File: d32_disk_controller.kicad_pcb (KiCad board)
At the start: 2 copper layers, 136.4 x 80.3 mm, 25 parts, among them J1 Clock_Test, J2 IDC_Floppy, J3 EDGE, U1 27C64, U2 WD2797, U3 74LS174, U4 74LS139, U5 74LS00, U6 7416, U7 7417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

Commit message: redraft traces
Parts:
- moved U7 39.7 mm to (122.9, 62.5)
- moved U6 31.8 mm to (131.6, 75.2)
- moved RN1 31.2 mm to (140.5, 71.4)
- moved J2 29.0 mm to (145.8, 62.0)
- moved U2 28.5 mm to (102.9, 70.6)
- moved U8 24.8 mm to (122.9, 51.3)
- moved R9 18.3 mm to (125.5, 89.9)
- moved C7 17.8 mm to (130.0, 110.7)
- moved U1 15.5 mm to (72.9, 85.3)
- moved C2 10.2 mm to (129.5, 105.2), turned to 0 degrees
- moved J1 8.84 mm to (136.9, 93.5)
- moved R8 8.78 mm to (131.6, 92.5), turned to 0 degrees
- moved R10 8.35 mm to (125.5, 99.8)
- moved D1 5.89 mm to (131.6, 100.6)
- moved R3 4.86 mm to (131.6, 97.2)
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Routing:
- net GND: track 593.4 -> 102.1 mm, vias 2 -> 5
- net +5V: track 353.3 -> 0.00 mm, vias 11 -> 0
- net ~{NMI}: track 162.0 -> 0.00 mm, vias 1 -> 0
- net P2: track 141.8 -> 0.00 mm, vias 1 -> 0
- net D0: track 138.4 -> 0.00 mm, vias 2 -> 0
- net D3: track 135.5 -> 0.00 mm, vias 2 -> 0
- net D4: track 132.8 -> 0.00 mm, vias 1 -> 0
- net MOTOR: track 131.6 -> 0.00 mm, vias 1 -> 0
- net D5: track 130.3 -> 0.00 mm, vias 2 -> 0
- net D2: track 127.1 -> 0.00 mm, vias 2 -> 0
- net D1: track 120.5 -> 0.00 mm, vias 3 -> 0
- net D6: track 112.1 -> 0.00 mm, vias 1 -> 0
- net D7: track 106.0 -> 0.00 mm, vias 2 -> 0
- net Net-(U3-Q2): track 105.3 -> 0.00 mm, vias 2 -> 0
- net Net-(U5-Pad3): track 99.8 -> 0.00 mm, vias 4 -> 0
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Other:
- board size 136.4 x 80.3 mm -> 107.5 x 80.3 mm

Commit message: rework traces
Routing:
- net +5V: track 0.00 -> 412.3 mm, vias 0 -> 19
- net GND: track 102.1 -> 353.6 mm, vias 5 -> 17
- net ~{RESET}: track 0.00 -> 105.3 mm, vias 0 -> 5
- net MOTOR: track 0.00 -> 88.7 mm, vias 0 -> 6
- net Net-(U3-Q2): track 0.00 -> 82.6 mm, vias 0 -> 6
- net STEP: track 0.00 -> 74.4 mm, vias 0 -> 3
- net ~{WPRT}: track 0.00 -> 74.0 mm, vias 0 -> 4
- net CLK: track 0.00 -> 65.7 mm, vias 0 -> 2
- net DIRC: track 0.00 -> 59.9 mm, vias 0 -> 1
- net D1: track 0.00 -> 56.8 mm, vias 0 -> 2
- net D0: track 0.00 -> 56.7 mm, vias 0 -> 2
- net D2: track 0.00 -> 56.6 mm, vias 0 -> 2
- net ~{IP}: track 0.00 -> 55.4 mm, vias 0 -> 4
- net Net-(U4A-O3): track 0.00 -> 54.6 mm, vias 0 -> 4
- net /raw_clock: track 0.00 -> 52.4 mm, vias 0 -> 4
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
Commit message: revise tracing
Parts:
- moved C1 8.65 mm to (86.1, 68.1)
- moved Y1 1.02 mm to (91.2, 68.0)
- moved R1 0.93 mm to (96.7, 70.1)
- moved R2 0.73 mm to (96.8, 62.5)
- moved C8 0.20 mm to (96.7, 66.3)
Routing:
- net GND: track 353.6 -> 511.2 mm, vias 17 -> 27
- net P2: track 0.00 -> 115.7 mm, vias 0 -> 3
- net R/~{W}: track 0.00 -> 85.5 mm, vias 0 -> 3
- net A3: track 31.2 -> 108.1 mm, vias 3 -> 6
- net CART: track 0.00 -> 73.3 mm, vias 0 -> 3
- net INTR0: track 0.00 -> 72.8 mm, vias 0 -> 4
- net D5: track 28.8 -> 99.2 mm, vias 2 -> 5
- net D4: track 33.7 -> 101.7 mm, vias 2 -> 6
- net D0: track 56.7 -> 122.4 mm, vias 2 -> 6
- net D3: track 39.2 -> 103.7 mm, vias 2 -> 5
- net D1: track 56.8 -> 121.0 mm, vias 2 -> 5
- net D2: track 56.6 -> 119.8 mm, vias 2 -> 6
- net ~{NMI}: track 0.00 -> 62.9 mm, vias 0 -> 1
- net +5V: track 412.3 -> 472.4 mm, vias 19 -> 26
- net D6: track 24.3 -> 81.3 mm, vias 2 -> 4
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
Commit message: verify component availability
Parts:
- U3: value 74LS174 -> 74HCT174; footprint Package_SO:SOIC-16W_7.5x10.3mm_P1.27mm -> Package_SO:SOIC-16W_5.3x10.2mm_P1.27mm
- U4: value 74LS139 -> 74HCT139; footprint Package_SO:SOIC-16W_7.5x10.3mm_P1.27mm -> Package_SO:SOIC-16W_5.3x10.2mm_P1.27mm
- U5: value 74LS00 -> 74HCT00; footprint Package_SO:SOIC-14W_7.5x9mm_P1.27mm -> Package_SO:SOIC-14_3.9x8.7mm_P1.27mm
- U6: value 7416 -> 74HCT04; footprint Package_SO:SOIC-14W_7.5x9mm_P1.27mm -> Package_SO:SOIC-14_3.9x8.7mm_P1.27mm
- U7: value 7417 -> 74LS07; footprint Package_SO:SOIC-14W_7.5x9mm_P1.27mm -> Package_SO:SOIC-14_3.9x8.7mm_P1.27mm
- U8: value 74LS74 -> 74HCT74; footprint Package_SO:SOIC-14W_7.5x9mm_P1.27mm -> Package_SO:SOIC-14_3.9x8.7mm_P1.27mm
- U9: value 74LS04 -> 74HCT04; footprint Package_SO:SOIC-14W_7.5x9mm_P1.27mm -> Package_SO:SOIC-14_3.9x8.7mm_P1.27mm
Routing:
- net GND: track 511.2 -> 525.5 mm
- net Net-(U8A-C): track 16.1 -> 10.0 mm
- net Net-(U5-Pad12): track 7.61 -> 12.0 mm
- net CLK: track 65.7 -> 70.1 mm
- net Net-(U5-Pad9): track 12.2 -> 16.5 mm
- net Net-(U3-Q1): track 54.9 -> 59.2 mm, vias 4 -> 2
- net Net-(U4B-O2): track 43.5 -> 39.3 mm
- net INT: track 22.5 -> 18.5 mm
- net Q: track 45.1 -> 42.0 mm, vias 4 -> 2
- net Net-(U4A-O3): track 53.3 -> 50.6 mm
- net INTR0: track 72.8 -> 70.1 mm
- net Net-(U3-Cp): track 26.0 -> 28.7 mm
- net Net-(U4A-O0): track 44.2 -> 41.6 mm
- net Net-(U4A-O2): track 25.1 -> 27.6 mm
- net DS1: track 27.9 -> 30.2 mm
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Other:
- board text added: "Dragon 32/64 Disk Controller"
- board text added: "V0.0.2-draft"

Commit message: update version
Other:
- board text added: "V0.0.3-draft"
- board text removed: "V0.0.2-draft"
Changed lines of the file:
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@@
     (title "Dragon 32/64 Disk Controller")
     (date "2023-07-06")
-    (rev "V0.0.2")
+    (rev "V0.0.3-draft")
   )
   (layers
@@
   (gr_line (start 63.6524 110.4392) (end 64.2112 110.4392)
     (stroke (width 0.1) (type default)) (layer "Edge.Cuts"))
-  (gr_text "V0.0.2-draft" (at 130.048 51.054) (layer "F.SilkS")
+  (gr_text "V0.0.3-draft" (at 130.048 51.054) (layer "F.SilkS")
     (effects (font (size 1 1) (thickness 0.15)) (justify left bottom))
   )

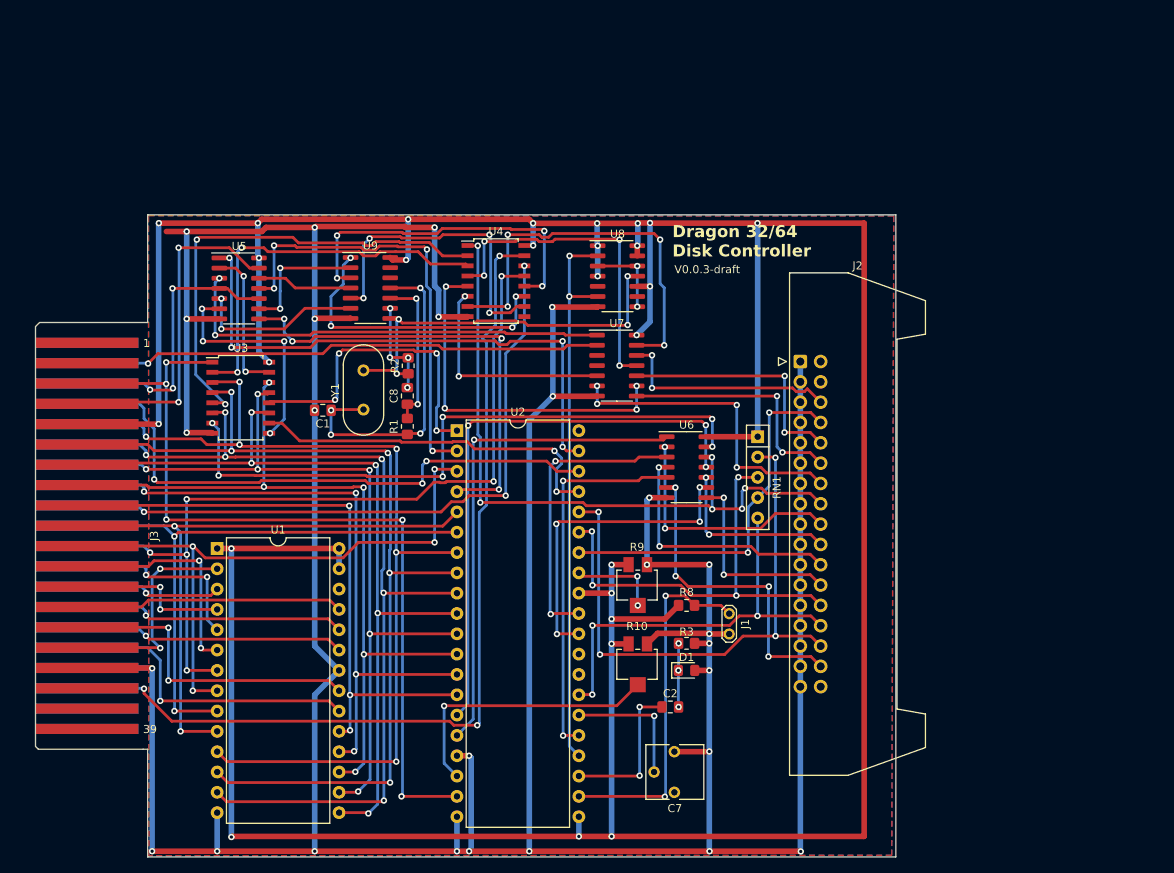
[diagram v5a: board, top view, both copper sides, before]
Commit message: revise board for better component selection
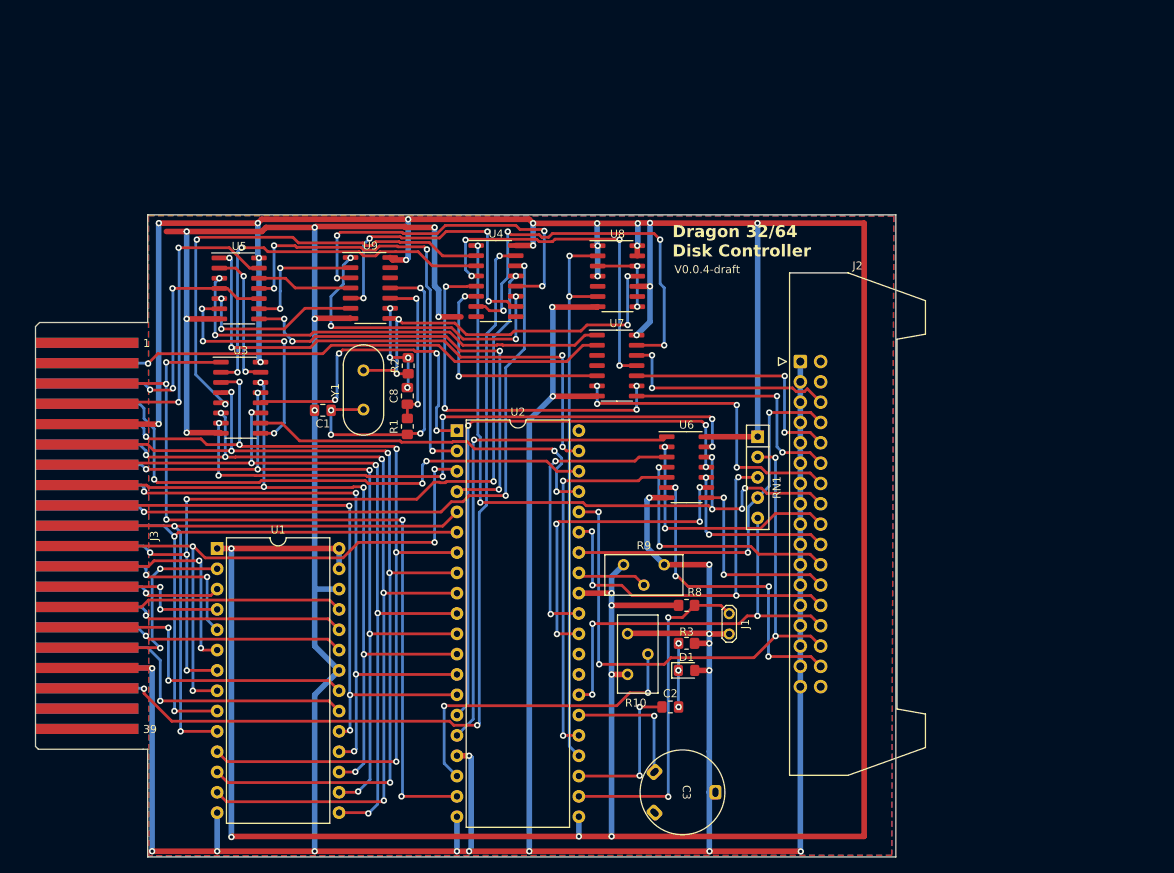
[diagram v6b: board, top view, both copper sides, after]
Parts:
- removed C7: 8-70pF, Potentiometer_THT:Potentiometer_Vishay_T73YP_Vertical
- added C3: 5.5-65pf, d32_cart:Trimmer-10mm, F.Cu at (131.1, 115.8)
- R10, R9: footprint Potentiometer_SMD:Potentiometer_Bourns_3224X_Vertical -> Potentiometer_THT:Potentiometer_Bourns_3296Y_Vertical
- U3, U4: footprint Package_SO:SOIC-16W_5.3x10.2mm_P1.27mm -> Package_SO:SOIC-16_3.9x9.9mm_P1.27mm
- moved R9 4.17 mm to (128.8, 87.4)
- moved R10 4.03 mm to (124.2, 96.0), turned to 90 degrees
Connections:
- U1 pad 26: unconnected-(U1-NC-Pad26) -> GND
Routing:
- net Net-(U2-RPW): track 34.7 -> 40.4 mm, vias 1 -> 2
- net ~{TEST}: track 44.8 -> 42.3 mm
- net Net-(U2-WPW): track 11.2 -> 8.76 mm, vias 2 -> 0
- net Net-(U4B-O2): track 39.3 -> 37.1 mm
- net A3: track 106.4 -> 104.3 mm
- net ~{WPRT}: track 74.0 -> 75.8 mm
- net D2: track 118.7 -> 117.0 mm
- net P2: track 114.4 -> 112.9 mm
- net Net-(U3-Cp): track 28.7 -> 30.2 mm
- net Net-(U4A-O2): track 27.6 -> 29.0 mm
- net ~{NMI}: track 65.1 -> 66.4 mm
- net MOTOR: track 86.8 -> 85.6 mm
- net Net-(U4A-O0): track 41.6 -> 42.8 mm
- net Net-(U4B-O1): track 37.6 -> 38.8 mm
- net ~{RE}: track 57.3 -> 56.0 mm
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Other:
- board text added: "V0.0.4-draft"
- board text removed: "V0.0.3-draft"

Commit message: prepare for cpld
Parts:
- removed C1: 22pF, Capacitor_SMD:C_0805_2012Metric_Pad1.18x1.45mm_HandSolder
- removed C8: 10nF, Capacitor_SMD:C_0805_2012Metric_Pad1.18x1.45mm_HandSolder
- removed R1, R2: 1K, Resistor_SMD:R_0805_2012Metric_Pad1.20x1.40mm_HandSolder
- Y1: footprint Crystal:Crystal_HC18-U_Vertical -> Oscillator:Oscillator_SMD_Abracon_ASV-4Pin_7.0x5.1mm
- moved Y1 53.5 mm to (129.6, 30.6)
- moved C2 25.9 mm to (129.2, 79.2), turned to 180 degrees
- moved C3 25.5 mm to (128.7, 90.4)
- moved J1 24.9 mm to (134.5, 68.7)
- moved R9 24.9 mm to (126.4, 62.6)
- moved U3 24.9 mm to (73.5, 41.7)
- moved J2 24.9 mm to (143.4, 37.2)
- moved J3 24.9 mm to (63.1, 59.0)
- moved U4 24.9 mm to (105.4, 27.1)
- moved U5 24.9 mm to (73.3, 28.0)
- moved U7 24.9 mm to (120.5, 37.7)
- moved U8 24.9 mm to (120.5, 26.5)
- moved U9 24.9 mm to (89.7, 28.0)
- moved R10 24.9 mm to (121.8, 71.2)
- moved U1 24.9 mm to (70.5, 60.5)
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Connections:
- J3 pad 37: unconnected-(J3-Pin_37-Pad37) -> A13
- RN1 pad 2: ~{WPRT} -> ~{IP}
- RN1 pad 3: ~{IP} -> ~{TR00}
- RN1 pad 4: ~{TR00} -> ~{WPRT}
- U1 pad 26: GND -> A13
- U9 pad 10: Net-(C8-Pad1) -> unconnected-(U9-Pad10)
- U9 pad 11: Net-(C1-Pad1) -> unconnected-(U9-Pad11)
- U9 pad 8: /raw_clock -> unconnected-(U9-Pad8)
- U9 pad 9: Net-(C8-Pad2) -> unconnected-(U9-Pad9)
- Y1 pad 1: Net-(C1-Pad1) -> unconnected-(Y1-EN-Pad1)
- Y1 pad 2: /raw_clock -> GND
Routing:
- net GND: track 524.7 -> 32.1 mm, vias 25 -> 11
- net +5V: track 473.7 -> 30.4 mm, vias 25 -> 14
- net A13: track 0.00 -> 52.4 mm, vias 0 -> 2
- net /raw_clock: track 51.1 -> 5.19 mm, vias 4 -> 0
- net Net-(C1-Pad1): track 40.8 -> 0.00 mm, vias 4 -> 0
- net Net-(C8-Pad1): track 19.6 -> 0.00 mm, vias 2 -> 0
- net ENP: track 40.5 -> 26.0 mm, vias 4 -> 0
- net Net-(C8-Pad2): track 12.3 -> 0.00 mm, vias 4 -> 0
- net Net-(U4A-O3): track 50.7 -> 62.7 mm, vias 4 -> 2
- net ~{WPRT}: track 75.8 -> 65.2 mm, vias 4 -> 1
- net Net-(U3-Q2): track 80.2 -> 89.1 mm, vias 6 -> 4
- net Net-(U2-RPW): track 40.4 -> 31.7 mm, vias 2 -> 0
- net ~{SSO}: track 40.2 -> 32.1 mm, vias 4 -> 1
- net WG: track 39.7 -> 32.0 mm, vias 4 -> 3
- net WD: track 37.1 -> 29.6 mm, vias 2 -> 1
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- added copper zone on In2.Cu, net +5V
- added copper zone on In1.Cu, net GND
- removed copper zone on B.Cu, net GND
- removed copper zone on F.Cu, net GND
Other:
- copper layers 2 -> 4
- board text added: "V0.0.5-draft"
- board text removed: "V0.0.4-draft"

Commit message: convert to small CPLD
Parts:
- removed U3: 74HCT174, Package_SO:SOIC-16_3.9x9.9mm_P1.27mm
- removed U4: 74HCT139, Package_SO:SOIC-16_3.9x9.9mm_P1.27mm
- removed U5: 74HCT00, Package_SO:SOIC-14_3.9x8.7mm_P1.27mm
- removed U7: 74LS07, Package_SO:SOIC-14_3.9x8.7mm_P1.27mm
- removed U8: 74HCT74, Package_SO:SOIC-14_3.9x8.7mm_P1.27mm
- removed U9: 74HCT04, Package_SO:SOIC-14_3.9x8.7mm_P1.27mm
- added C4: 100nF, Capacitor_SMD:C_0402_1005Metric, F.Cu at (84.2, 35.4)
- added C5: 100nF, Capacitor_SMD:C_0402_1005Metric, F.Cu at (91.8, 40.6)
- added C6: 100nF, Capacitor_SMD:C_0402_1005Metric, F.Cu at (99.9, 32.3)
- added C7: 100nF, Capacitor_SMD:C_0402_1005Metric, F.Cu at (90.5, 25.3)
- added J4: JTAG, Connector_PinHeader_2.54mm:PinHeader_2x05_P2.54mm_Vertical, F.Cu at (107.1, 27.2)
- added U10: ATF1504AS-xAx44, Package_QFP:TQFP-44_10x10mm_P0.8mm, F.Cu at (92.2, 33.0)
- moved Y1 55.6 mm to (74.0, 29.2), turned to 0 degrees
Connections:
- U6 pad 12: MOTOR -> (no net)
- U6 pad 13: Net-(U3-Q2) -> (no net)
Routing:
- net Net-(U3-Q2): track 89.1 -> 0.00 mm, vias 4 -> 0
- net Net-(U4A-O3): track 62.7 -> 0.00 mm, vias 2 -> 0
- net Net-(U5-Pad3): track 61.1 -> 0.00 mm, vias 2 -> 0
- net Net-(U3-Q1): track 60.3 -> 0.00 mm, vias 2 -> 0
- net ~{RESET}: track 107.2 -> 155.6 mm, vias 3 -> 5
- net Net-(U3-Q0): track 48.3 -> 0.00 mm, vias 2 -> 0
- net Net-(U4B-O0): track 45.3 -> 0.00 mm, vias 4 -> 0
- net DS1: track 29.7 -> 73.1 mm
- net INTR0: track 67.3 -> 25.1 mm, vias 3 -> 1
- net Net-(U4A-O1): track 41.9 -> 0.00 mm, vias 4 -> 0
- net DS2: track 36.3 -> 78.2 mm
- net ~{WE}: track 55.1 -> 14.7 mm, vias 4 -> 2
- net Net-(U4A-O0): track 39.7 -> 0.00 mm, vias 2 -> 0
- net TDI: track 0.00 -> 38.8 mm, vias 0 -> 1
- net Net-(U4B-O2): track 38.1 -> 0.00 mm, vias 4 -> 0
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- added copper zone on F.Cu, net GND
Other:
- board size 107.5 x 80.3 mm -> 107.5 x 74.2 mm
